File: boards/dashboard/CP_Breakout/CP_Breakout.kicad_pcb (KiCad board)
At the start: 2 copper layers, 7 parts, among them J1 M10LOCK, J11 M10LOCK, J12 M10LOCK, J2 M10LOCK, U1 CP2120

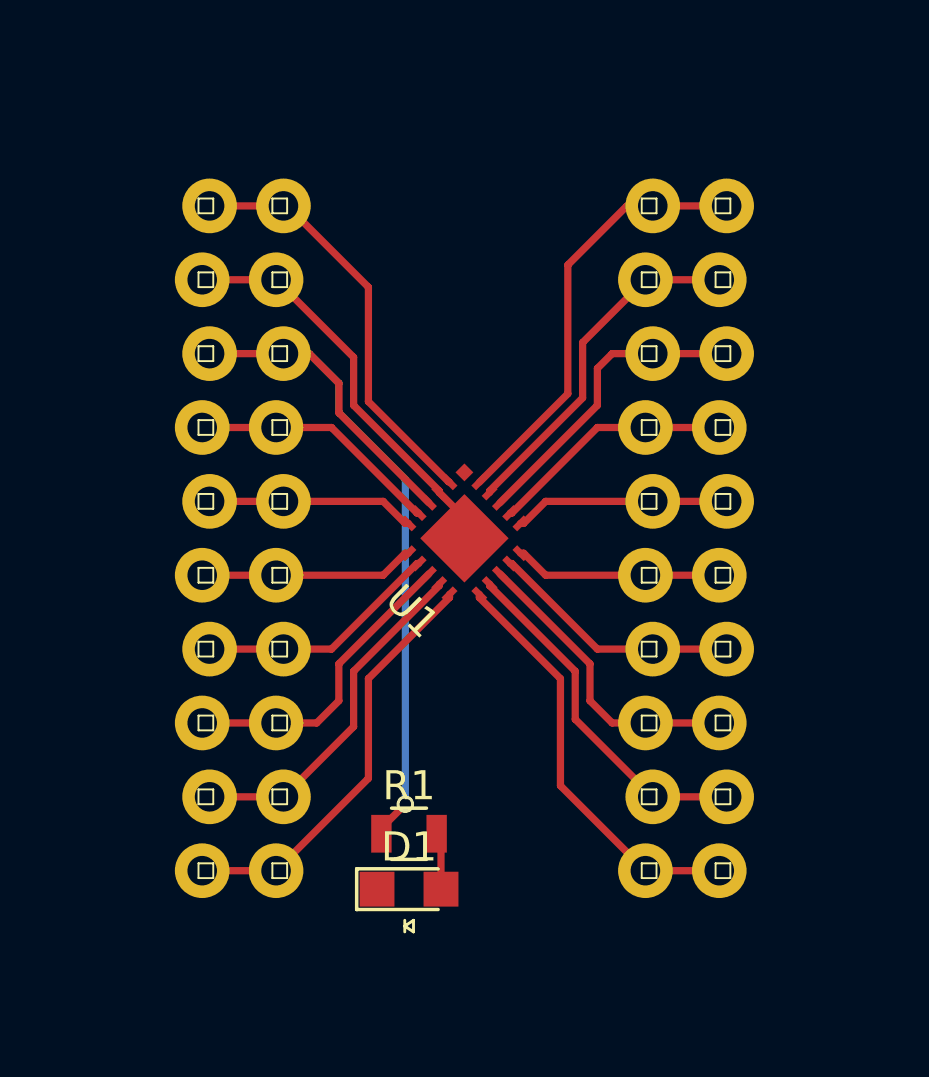
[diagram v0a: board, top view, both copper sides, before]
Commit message: Traces fixed on first draft breakout board
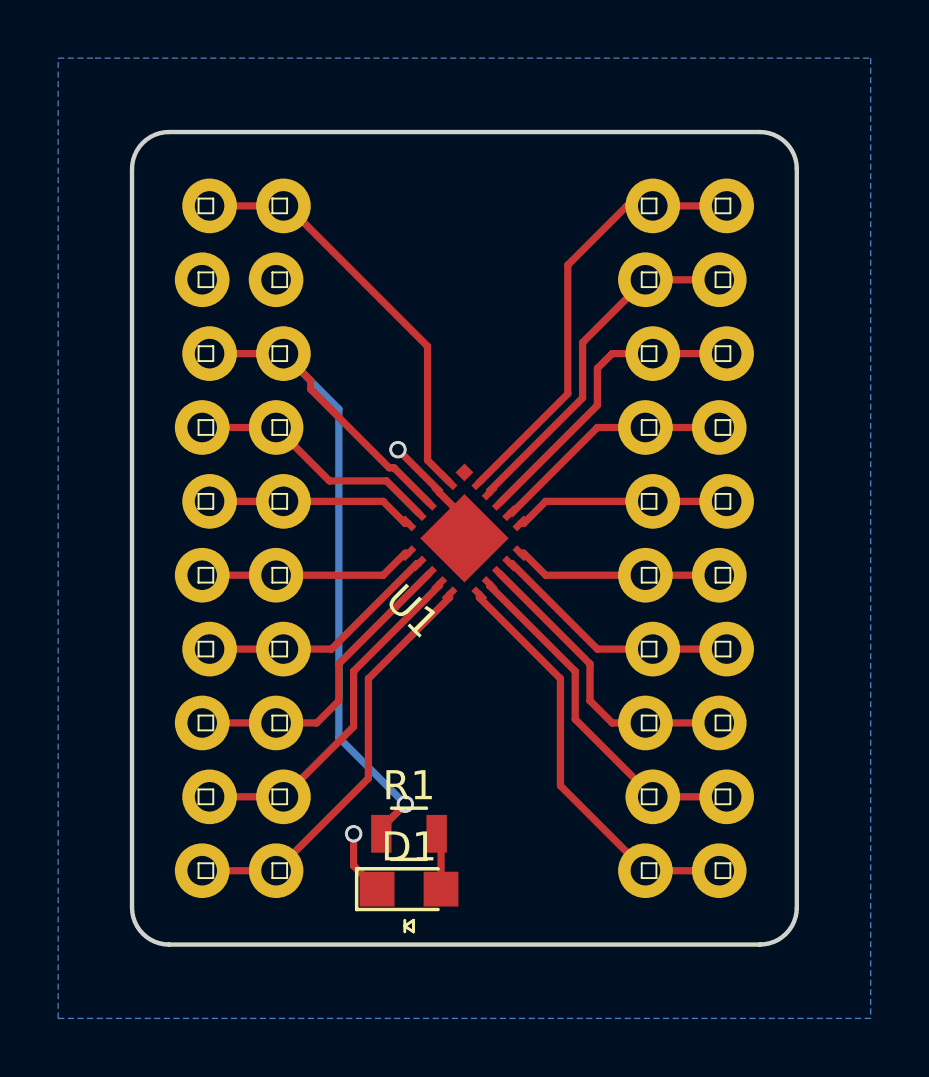
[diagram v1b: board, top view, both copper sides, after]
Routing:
- net /GND: track 14.2 -> 6.30 mm, vias 0 -> 2
- net Net-(J1-Pad8): track 29.4 -> 28.5 mm
- added copper zone on B.Cu, net /GND
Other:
- board outline added: 22.9 x 27.9 mm
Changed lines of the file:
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@@
   (general
     (links 44)
-    (no_connects 1)
+    (no_connects 0)
     (area 176.7237 105.108399 201.9268 133.282)
     (thickness 1.6)
-    (drawings 0)
-    (tracks 118)
+    (drawings 8)
+    (tracks 120)
     (zones 0)
     (modules 7)
@@
     (last_trace_width 0.25)
     (trace_clearance 0.2)
-    (zone_clearance 0.508)
+    (zone_clearance 0)
     (zone_45_only no)
     (trace_min 0.2)
@@
     )
   )
+  (gr_arc (start 179.07 130.81) (end 179.07 132.08) (angle 90) (layer Edge.Cuts) (width 0.15))
+  (gr_arc (start 199.39 130.81) (end 200.66 130.81) (angle 90) (layer Edge.Cuts) (width 0.15))
+  (gr_arc (start 199.39 105.41) (end 199.39 104.14) (angle 90) (layer Edge.Cuts) (width 0.15))
+  (gr_arc (start 179.07 105.41) (end 177.8 105.41) (angle 90) (layer Edge.Cuts) (width 0.15))
+  (gr_line (start 199.39 104.14) (end 179.07 104.14) (layer Edge.Cuts) (width 0.15))
+  (gr_line (start 200.66 130.81) (end 200.66 105.41) (layer Edge.Cuts) (width 0.15))
+  (gr_line (start 179.07 132.08) (end 199.39 132.08) (layer Edge.Cuts) (width 0.15))
+  (gr_line (start 177.8 105.41) (end 177.8 130.81) (layer Edge.Cuts) (width 0.15))
+  (segment (start 188.363794 116.481794) (end 186.944 115.062) (width 0.25) (layer F.Cu) (net 1))
+  (via (at 186.944 115.062) (size 0.6) (drill 0.4) (layers F.Cu B.Cu) (net 1))
+  (segment (start 188.363794 116.536687) (end 188.363794 116.481794) (width 0.25) (layer F.Cu) (net 1))
+  (segment (start 186.225 130.175) (end 185.42 129.37) (width 0.25) (layer F.Cu) (net 1))
+  (segment (start 185.42 129.37) (end 185.42 128.27) (width 0.25) (layer F.Cu) (net 1))
+  (via (at 185.42 128.27) (size 0.6) (drill 0.4) (layers F.Cu B.Cu) (net 1))
   (segment (start 189.23 118.11) (end 189.23 117.402893) (width 0.25) (layer F.Cu) (net 1))
   (segment (start 189.23 117.402893) (end 188.363794 116.536687) (width 0.25) (layer F.Cu) (net 1))
-  (segment (start 188.363794 116.536687) (end 188.363794 116.481794) (width 0.25) (layer F.Cu) (net 1))
-  (segment (start 188.363794 116.481794) (end 185.42 113.538) (width 0.25) (layer F.Cu) (net 1))
-  (segment (start 185.42 111.887) (end 182.753 109.22) (width 0.25) (layer F.Cu) (net 1))
-  (segment (start 185.42 113.538) (end 185.42 111.887) (width 0.25) (layer F.Cu) (net 1))
-  (segment (start 182.753 109.22) (end 180.213 109.22) (width 0.25) (layer F.Cu) (net 1))
   (segment (start 182.753 109.22) (end 182.82 109.22) (width 0.25) (layer F.Cu) (net 1))
   (segment (start 189.742652 120.036866) (end 189.742652 120.146652) (width 0.25) (layer F.Cu) (net 2))
@@
   (segment (start 183.007 116.84) (end 180.467 116.84) (width 0.25) (layer F.Cu) (net 9))
   (segment (start 183.007 116.84) (end 183.007 116.833) (width 0.25) (layer F.Cu) (net 9))
-  (segment (start 187.656687 117.243794) (end 187.601794 117.243794) (width 0.25) (layer F.Cu) (net 10))
-  (segment (start 187.601794 117.243794) (end 184.658 114.3) (width 0.25) (layer F.Cu) (net 10))
-  (segment (start 184.658 114.3) (end 182.753 114.3) (width 0.25) (layer F.Cu) (net 10))
+  (segment (start 186.549906 116.137013) (end 184.590013 116.137013) (width 0.25) (layer F.Cu) (net 10))
+  (segment (start 187.656687 117.243794) (end 186.549906 116.137013) (width 0.25) (layer F.Cu) (net 10))
+  (segment (start 184.590013 116.137013) (end 183.692799 115.239799) (width 0.25) (layer F.Cu) (net 10))
+  (segment (start 183.692799 115.239799) (end 182.753 114.3) (width 0.25) (layer F.Cu) (net 10))
   (segment (start 182.753 114.3) (end 180.34 114.3) (width 0.25) (layer F.Cu) (net 10))
   (segment (start 180.34 114.3) (end 180.213 114.3) (width 0.25) (layer F.Cu) (net 10))
   (segment (start 182.753 114.3) (end 182.753 114.287) (width 0.25) (layer F.Cu) (net 10))
-  (segment (start 186.375 128.27) (end 186.375 128.077) (width 0.25) (layer F.Cu) (net 11) (status C00000))
-  (segment (start 186.375 128.077) (end 187.198 127.254) (width 0.25) (layer F.Cu) (net 11) (status 400000))
+  (segment (start 183.946799 112.699799) (end 183.007 111.76) (width 0.25) (layer F.Cu) (net 11))
+  (segment (start 183.946799 112.989803) (end 183.946799 112.699799) (width 0.25) (layer F.Cu) (net 11))
+  (segment (start 186.643998 115.687002) (end 183.946799 112.989803) (width 0.25) (layer F.Cu) (net 11))
+  (segment (start 186.807002 115.687002) (end 186.643998 115.687002) (width 0.25) (layer F.Cu) (net 11))
+  (segment (start 184.912 124.968) (end 184.912 113.665) (width 0.25) (layer B.Cu) (net 11))
+  (segment (start 188.010241 116.890241) (end 186.807002 115.687002) (width 0.25) (layer F.Cu) (net 11))
+  (segment (start 187.198 127.254) (end 184.912 124.968) (width 0.25) (layer B.Cu) (net 11))
+  (segment (start 184.912 113.665) (end 183.946799 112.699799) (width 0.25) (layer B.Cu) (net 11))
+  (segment (start 183.946799 112.699799) (end 183.007 111.76) (width 0.25) (layer B.Cu) (net 11))
+  (segment (start 186.375 128.27) (end 186.375 128.077) (width 0.25) (layer F.Cu) (net 11))
+  (segment (start 186.375 128.077) (end 187.198 127.254) (width 0.25) (layer F.Cu) (net 11))
   (via (at 187.198 127.254) (size 0.6) (drill 0.4) (layers F.Cu B.Cu) (net 11))
-  (segment (start 187.198 127.254) (end 187.198 116.078) (width 0.25) (layer B.Cu) (net 11))
-  (segment (start 187.198 116.078) (end 184.912 113.792) (width 0.25) (layer B.Cu) (net 11))
-  (segment (start 184.912 113.792) (end 184.912 112.776) (width 0.25) (layer B.Cu) (net 11))
-  (segment (start 184.912 112.776) (end 183.896 111.76) (width 0.25) (layer B.Cu) (net 11) (status 800000))
-  (segment (start 183.896 111.76) (end 183.007 111.76) (width 0.25) (layer B.Cu) (net 11) (status C00000))
-  (segment (start 188.010241 116.890241) (end 184.912 113.792) (width 0.25) (layer F.Cu) (net 11))
-  (segment (start 184.912 112.776) (end 183.896 111.76) (width 0.25) (layer F.Cu) (net 11))
-  (segment (start 184.912 113.792) (end 184.912 112.776) (width 0.25) (layer F.Cu) (net 11))
-  (segment (start 183.896 111.76) (end 183.007 111.76) (width 0.25) (layer F.Cu) (net 11))
   (segment (start 183.007 111.76) (end 180.467 111.76) (width 0.25) (layer F.Cu) (net 11))
   (segment (start 183.007 111.76) (end 183.007 111.733) (width 0.25) (layer F.Cu) (net 11))
   (segment (start 183.007 106.68) (end 183.134 106.68) (width 0.25) (layer F.Cu) (net 12))
-  (segment (start 183.134 106.68) (end 185.928 109.474) (width 0.25) (layer F.Cu) (net 12))
-  (segment (start 185.928 113.409602) (end 188.681993 116.163595) (width 0.25) (layer F.Cu) (net 12))
-  (segment (start 185.928 109.474) (end 185.928 113.409602) (width 0.25) (layer F.Cu) (net 12))
-  (segment (start 188.681993 116.163595) (end 188.717348 116.183134) (width 0.25) (layer F.Cu) (net 12))
+  (segment (start 183.134 106.68) (end 187.96 111.506) (width 0.25) (layer F.Cu) (net 12))
+  (segment (start 187.96 111.506) (end 187.96 115.425786) (width 0.25) (layer F.Cu) (net 12))
+  (segment (start 187.96 115.425786) (end 188.452184 115.91797) (width 0.25) (layer F.Cu) (net 12))
+  (segment (start 188.452184 115.91797) (end 188.717348 116.183134) (width 0.25) (layer F.Cu) (net 12))
   (segment (start 183.007 106.68) (end 180.467 106.68) (width 0.25) (layer F.Cu) (net 12))
   (segment (start 183.007 106.68) (end 183.007 106.553) (width 0.25) (layer F.Cu) (net 12))
@@
   (segment (start 188.425 130.175) (end 188.425 128.42) (width 0.25) (layer F.Cu) (net 21))
   (segment (start 188.425 128.42) (end 188.275 128.27) (width 0.25) (layer F.Cu) (net 21))
+  (zone (net 1) (net_name /GND) (layer B.Cu) (hatch edge 0.508)
+    (connect_pads (clearance 0))
+    (min_thickness 0.254)
+    (fill yes (arc_segments 16) (thermal_gap 0.508) (thermal_bridge_width 0.508))
+    (polygon
+      (pts
+        (xy 176.53 101.6) (xy 203.2 101.6) (xy 203.2 134.62) (xy 175.26 134.62) (xy 175.26 101.6)
+      )
+    )
+  )
 )
